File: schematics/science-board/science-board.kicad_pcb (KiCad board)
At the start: 2 copper layers, 90.5 x 99.3 mm, 16 parts, among them J1 Conn_01x02, J10 Conn_01x04, J2 Conn_01x08, J3 Conn_01x04, J4 Conn_01x04, J5 Conn_01x08, J6 Conn_01x03, J7 Conn_01x08, J8 Conn_01x08, J9 Conn_01x04, U1 Teensy4.1, U2 LSF0108PWR

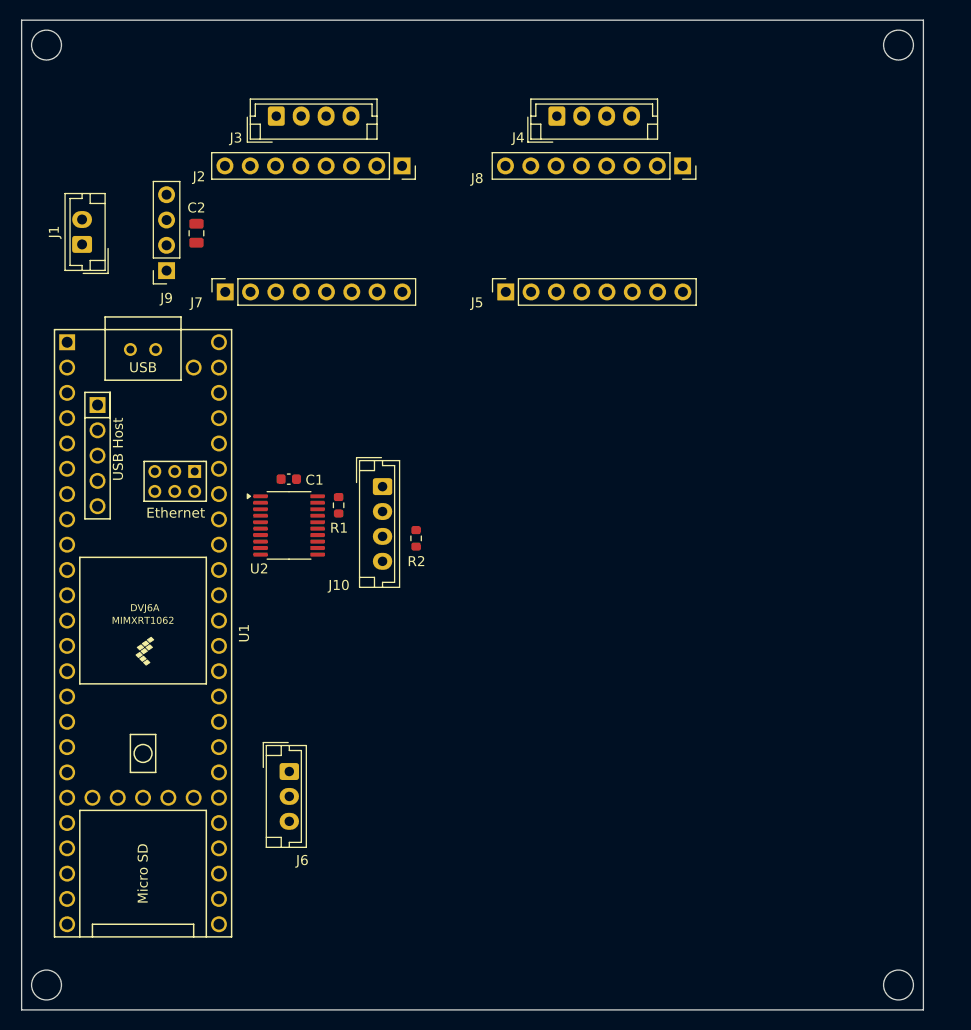
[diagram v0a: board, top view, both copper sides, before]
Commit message: Finished preliminary routing. Used through-hole footprints.
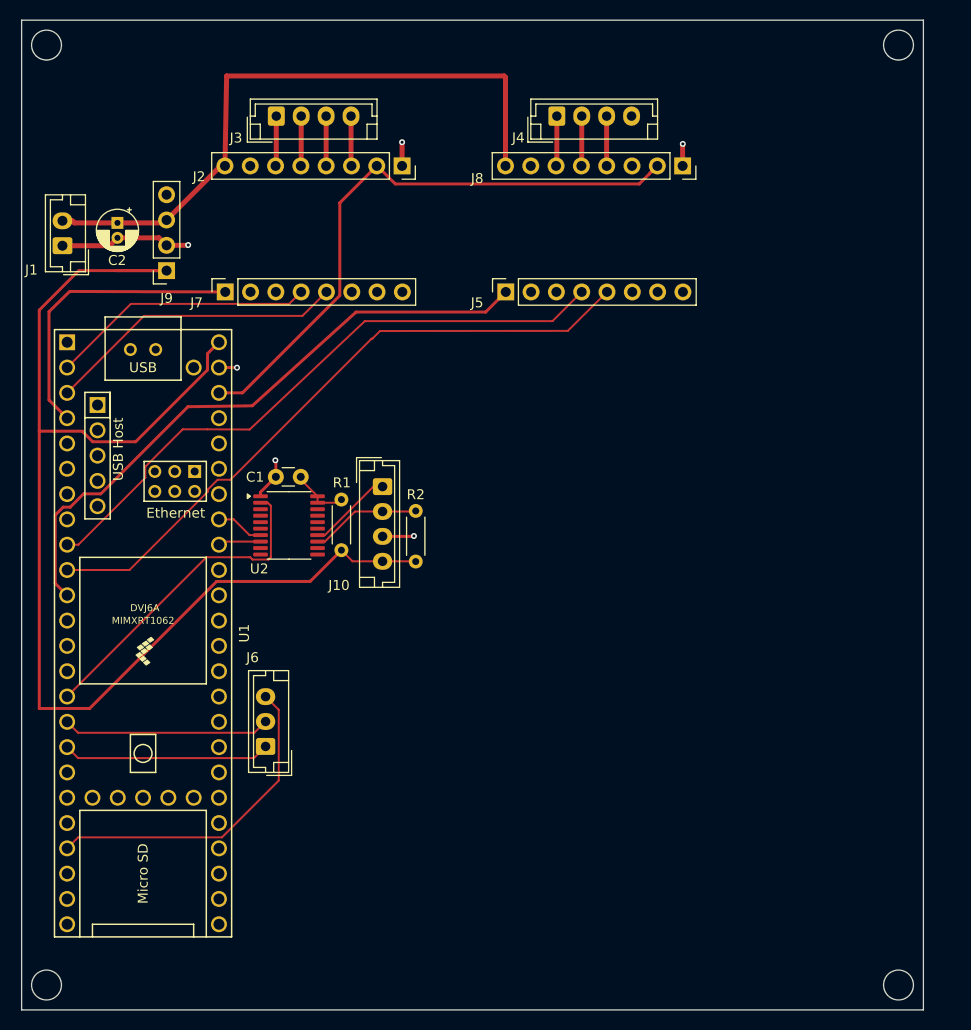
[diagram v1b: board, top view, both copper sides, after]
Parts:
- C1: footprint Capacitor_SMD:C_0603_1608Metric -> Capacitor_THT:C_Disc_D3.0mm_W1.6mm_P2.50mm
- C2: footprint Capacitor_SMD:C_0805_2012Metric -> Capacitor_THT:CP_Radial_D4.0mm_P1.50mm
- R1, R2: footprint Resistor_SMD:R_0603_1608Metric -> Resistor_THT:R_Axial_DIN0204_L3.6mm_D1.6mm_P5.08mm_Horizontal
- moved C2 8.00 mm to (25.6, 37.0)
- moved R1 4.51 mm to (48.0, 69.9)
- moved J6 3.47 mm to (40.4, 89.6), turned to 90 degrees
- moved R2 2.76 mm to (55.5, 65.9)
- moved J1 1.97 mm to (20.0, 39.3)
- moved C1 1.22 mm to (44.0, 62.5)
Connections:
- net Net-(U2-EN) renamed /EN
- U1 pad 15: unconnected-(U1-3V3-Pad15) -> +3.3V
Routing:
- net +5V: track 0.00 -> 127.9 mm
- net +3.3V: track 0.00 -> 94.3 mm
- net /D2_RX: track 0.00 -> 65.9 mm
- net +24V: track 0.00 -> 64.7 mm
- net /D2_EN: track 0.00 -> 62.7 mm
- net /D2_TX: track 0.00 -> 62.6 mm
- net /ENA: track 0.00 -> 33.0 mm
- net /D1_RX: track 0.00 -> 30.2 mm
- net /D1_EN: track 0.00 -> 29.9 mm
- net GND: track 0.00 -> 27.1 mm, vias 0 -> 6
- net /D1_TX: track 0.00 -> 26.6 mm
- net /EN1: track 0.00 -> 20.9 mm
- net /EN2: track 0.00 -> 20.8 mm
- net /Black/SDA: track 0.00 -> 11.1 mm
- net /Yellow/SCL: track 0.00 -> 8.54 mm
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
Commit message: Updated board measurements.
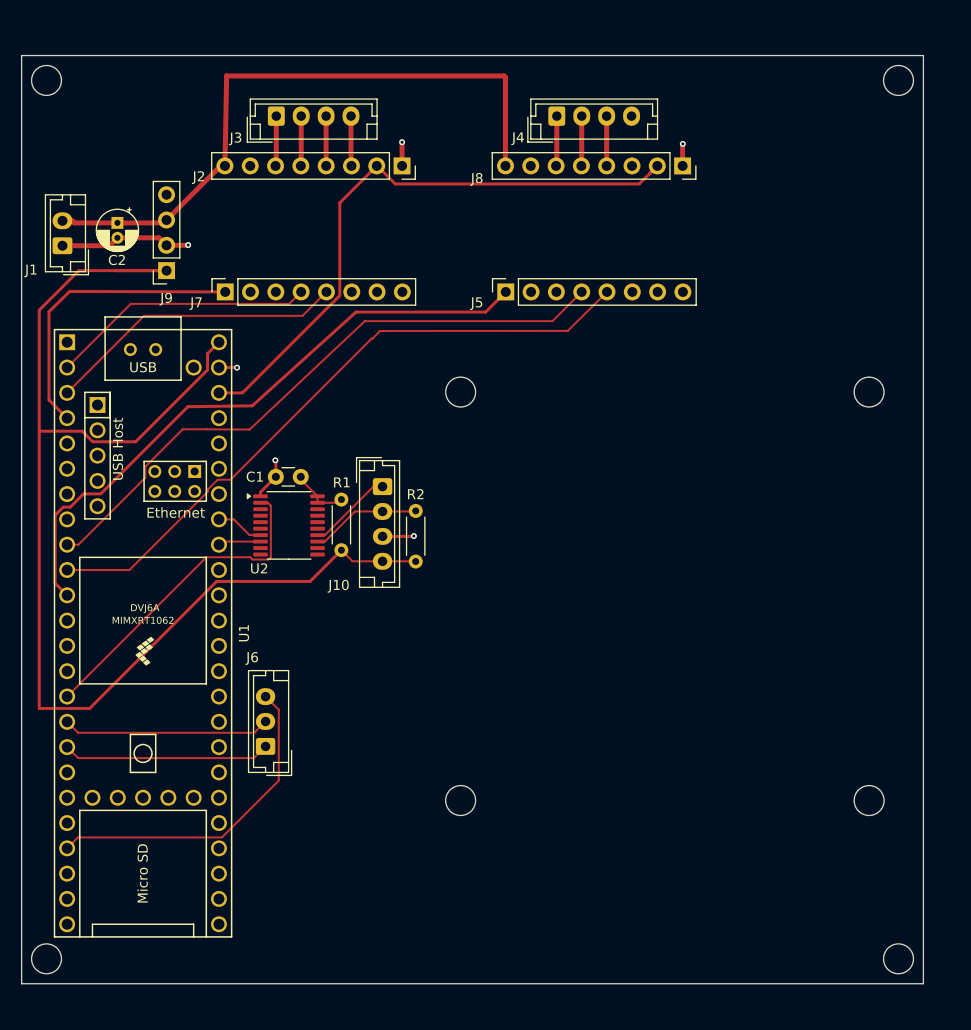
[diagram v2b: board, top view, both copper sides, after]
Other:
- board size 90.5 x 99.3 mm -> 90.5 x 93.2 mm
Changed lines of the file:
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@@
 	)
 	(gr_circle
-		(center 103.95 113.52)
-		(end 105.45 113.52)
+		(center 103.95 110.89)
+		(end 105.45 110.89)
 		(stroke
 			(width 0.05)
@@
 	)
 	(gr_circle
-		(center 18.43 113.52)
-		(end 19.93 113.52)
+		(center 18.43 110.89)
+		(end 19.93 110.89)
+		(stroke
+			(width 0.05)
+			(type default)
+		)
+		(fill none)
+		(layer "Edge.Cuts")
+	)
+	(gr_circle
+		(center 101 95)
+		(end 102.5 95)
+		(stroke
+			(width 0.05)
+			(type default)
+		)
+		(fill none)
+		(layer "Edge.Cuts")
+	)
+	(gr_circle
+		(center 60 54)
+		(end 61.5 54)
 		(stroke
 			(width 0.05)
@@
 	)
 	(gr_rect
-		(start 15.93 16.67)
-		(end 106.45 116.02)
+		(start 15.93 20.22)
+		(end 106.45 113.39)
 		(stroke
 			(width 0.05)
@@
 	)
 	(gr_circle
-		(center 103.95 19.17)
-		(end 105.45 19.17)
+		(center 103.95 22.72)
+		(end 105.45 22.72)
 		(stroke
 			(width 0.05)
@@
 	)
 	(gr_circle
-		(center 18.43 19.17)
-		(end 19.93 19.17)
+		(center 18.43 22.72)
+		(end 19.93 22.72)
 		(stroke
 			(width 0.05)
+			(type default)
+		)
+		(fill none)
+		(layer "Edge.Cuts")
+	)
+	(gr_circle
+		(center 60 95)
+		(end 61.5 95)
+		(stroke
+			(width 0.05)
+			(type default)
+		)
+		(fill none)
+		(layer "Edge.Cuts")
+	)
+	(gr_circle
+		(center 101 54)
+		(end 102.5 54)
+		(stroke
+			(width 0.05)

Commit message: Added Ethernet module.
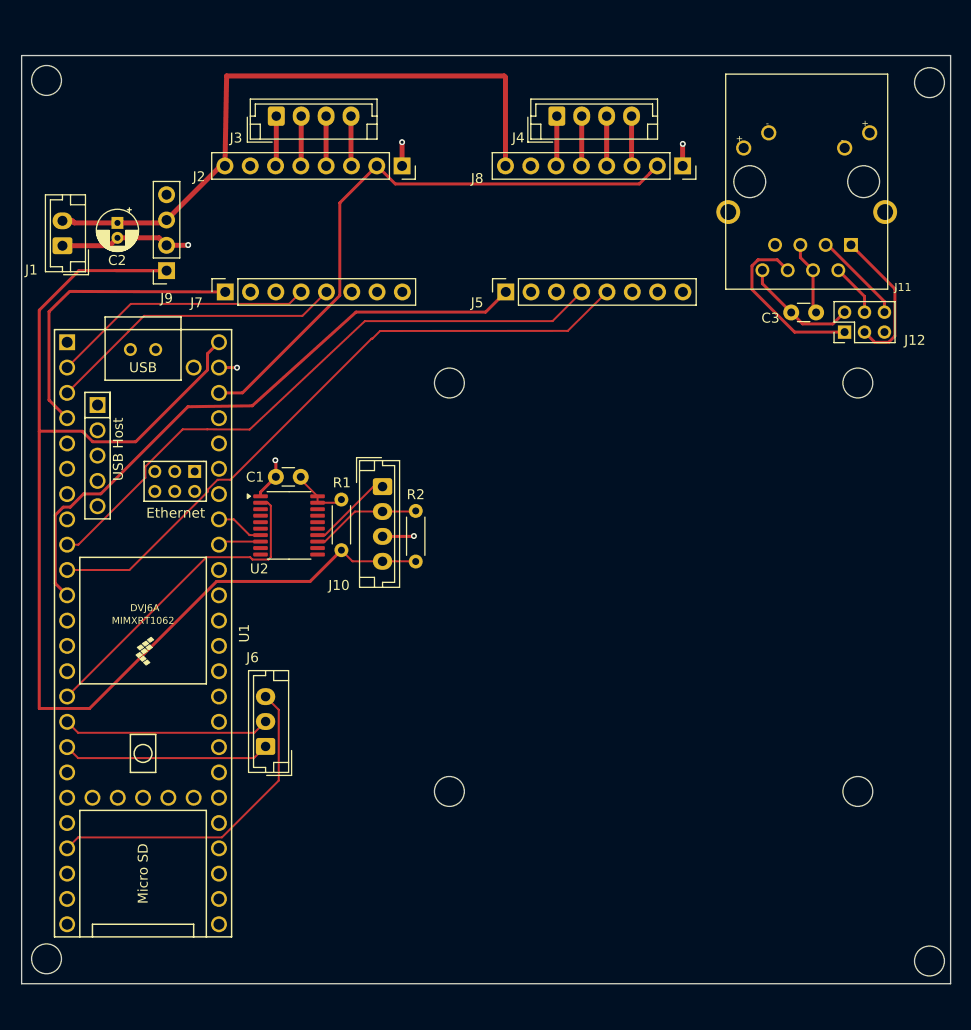
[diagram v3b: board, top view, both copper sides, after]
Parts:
- added C3: 0.1uF, Capacitor_THT:C_Disc_D3.0mm_W1.6mm_P2.50mm, F.Cu at (95.7, 46.0)
- added J11: J00-0045NL, J00-0045NL:PULSE_J00-0045NL, F.Cu at (94.7, 32.9)
- added J12: Conn_02x03_Counter_Clockwise, Connector_PinHeader_2.00mm:PinHeader_2x03_P2.00mm_Vertical, F.Cu at (98.5, 48.0)
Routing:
- net /RX-: track 0.00 -> 17.7 mm
- net /TX+: track 0.00 -> 14.7 mm
- net GND: track 27.1 -> 38.9 mm
- net /RX+: track 0.00 -> 9.32 mm
- net /CTR: track 0.00 -> 7.43 mm
- net /TX-: track 0.00 -> 5.30 mm
- net /D2_B2: track 0.00 -> 5.02 mm
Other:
- board size 90.5 x 93.2 mm -> 93.2 x 93.2 mm
